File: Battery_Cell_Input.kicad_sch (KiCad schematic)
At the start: 3 parts, among them J801 Conn_01x02, J802 Conn_01x02, J803 Conn_01x02

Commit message: specified design
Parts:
- removed J801, J802: Conn_01x02, symbol Connector_Generic:Conn_01x02
- added BT1101, BT1102, BT1103, BT1104: Battery_Cell, symbol Device:Battery_Cell
- added C1101, C1102: C_Small, Capacitor_SMD:C_0603_1608Metric_Pad1.08x0.95mm_HandSolder, symbol Device:C_Small
- added D1101, D1102: 1N4148WT, Diode_SMD:D_SOD-523, symbol Diode:1N4148WT
- added J1101: Battery_1, Connector_Harwin:Harwin_Gecko-G125-FVX1605L0X_2x08_P1.25mm_Vertical, symbol Connector_Generic:Conn_02x08_Row_Letter_Last
- added Q1101, Q1102: NMOS, Package_TO_SOT_SMD:SOT-23-6, symbol Simulation_SPICE:NMOS
- added R1101, R1102: TBD, Resistor_SMD:R_0603_1608Metric_Pad0.98x0.95mm_HandSolder, symbol Device:R_Small
- added R1103, R1104, R1105, R1106, R1107, R1108, R1109, R1110, R1111, R1112, R1113, R1114: R_Small, Resistor_SMD:R_0603_1608Metric_Pad0.98x0.95mm_HandSolder, symbol Device:R_Small
- added U1101: BQ76920PW, Package_SO:TSSOP-20_4.4x6.5mm_P0.65mm, symbol Battery_Management:BQ76920PW
- J1102: renamed from J803; symbol Connector_Generic:Conn_01x02 -> Connector_Generic:Conn_01x04
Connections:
- net Batt: now also BT1101.1 (+), D1101.2 (A), D1102.2 (A), R1107.1
- net GND: now also J1102.2 (Pin_2), C1101.2, C1102.2, J1101.3a (Pin_3a), J1101.3b (Pin_3b), J1101.4a (Pin_4a), J1101.4b (Pin_4b), J1101.6a (Pin_6a), J1101.6b (Pin_6b), Q1102.3 (S), R1101.1, R1102.1, R1109.2, R1114.2, U1101.3 (VSS)
- net Heater_EN: now also J1101.8a (Pin_8a), J1101.8b (Pin_8b)
- net VMEAS: now also J1101.7a (Pin_7a), J1101.7b (Pin_7b)
- new net: Q1101.3 (S), R1108.2, R1110.2, R1111.2
- new net: R1110.1, U1101.19 (SRN)
- new net: BT1103.2 (-), BT1104.1 (+), R1105.1
- new net: Q1101.1 (D), Q1102.1 (D)
- new net: BT1102.2 (-), BT1103.1 (+), R1104.1
- new net: BT1104.2 (-), R1106.1, R1108.1
- new net: BT1101.2 (-), BT1102.1 (+), R1103.1
- new net: C1101.1, R1112.2, U1101.9 (REGSRC)
- new net: D1102.1 (K), R1113.1
- new net: C1102.1, R1113.2, U1101.10 (BAT)
- new net: D1101.1 (K), R1112.1
- new net: R1107.2, U1101.13 (VC4)
- new net: R1109.1, U1101.17 (VC0)
- new net: R1106.2, U1101.18 (SRP)
- new net Batt_1: R1105.2, U1101.16 (VC1)
- new net Batt_2: R1104.2, U1101.15 (VC2)
- new net Batt_3: R1103.2, U1101.14 (VC3)
- new net CHG: Q1102.2 (G), R1114.1, U1101.2 (CHG)
- new net DSG: Q1101.2 (G), R1111.1, U1101.1 (DSG)
- new net Pack: J1101.1a (Pin_1a), J1101.1b (Pin_1b), J1101.2a (Pin_2a), J1101.2b (Pin_2b)
- new net Switch_Batt_Heater/ILIM_1: R1102.2
- new net Switch_Batt_Heater/ILIM_2: R1101.2
- new net Switch_Batt_Heater/VOUT: J1102.3 (Pin_3), J1102.4 (Pin_4)
- new net TMEAS: J1101.5a (Pin_5a), J1101.5b (Pin_5b)
- no-connect marks 0 -> 4
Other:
- added sheet Switch_Batt_Heater (Switch_H.kicad_sch)
- added sheet Temp_sens_battery (Temp_sens.kicad_sch)
- note added: "Current limiter"
- note removed: "Batt heater"
- note removed: "Charger"
- note removed: "Temp Sens Batt"
- note removed: "Temp Sens Charger"
- note removed: "Temp sens Conn"

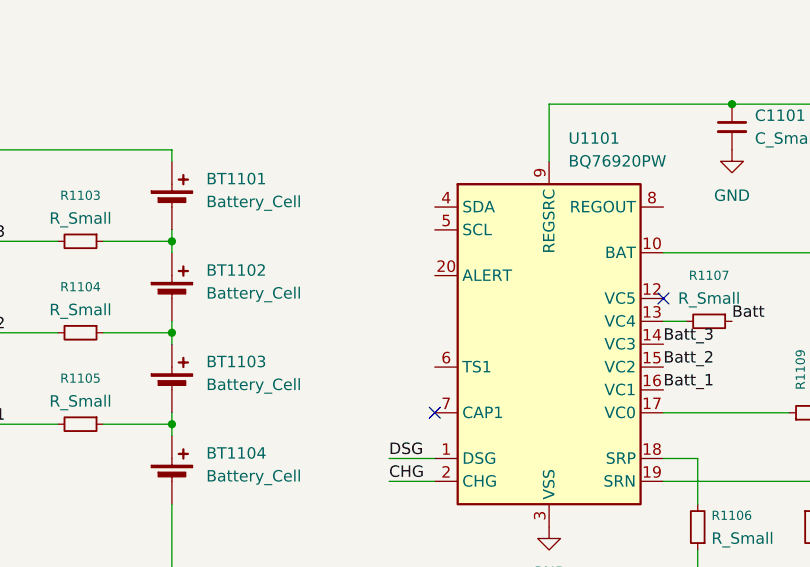
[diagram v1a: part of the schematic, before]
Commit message: added second AMUX and housekeeping
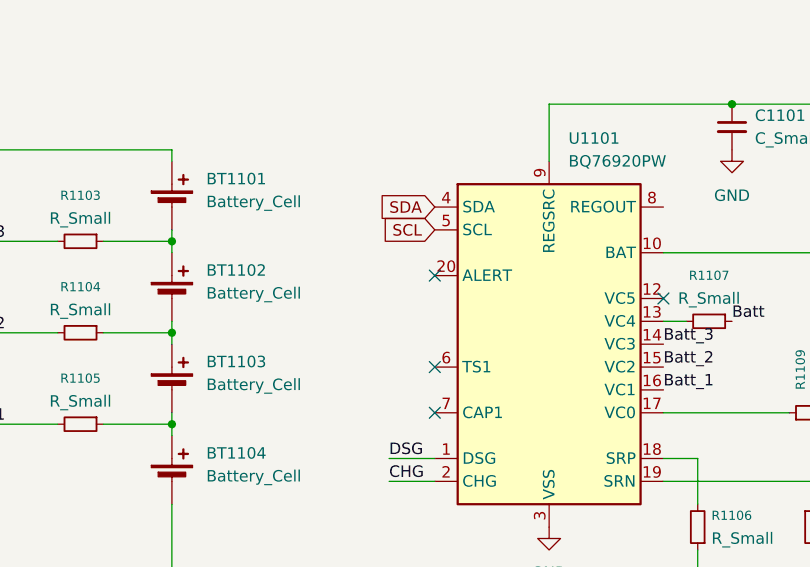
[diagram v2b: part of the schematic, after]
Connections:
- net SDA: now reaches U1101.4 (SDA)
- net SCL: now reaches U1101.5 (SCL)
- no-connect marks 4 -> 6
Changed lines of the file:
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@@
+	)
+	(no_connect
+		(at 175.26 113.03)
 	)
 	(no_connect
 		(at 175.26 128.27)
+	)
+	(no_connect
+		(at 175.26 123.19)
 	)
 	(no_connect
@@
 		)
 	)
+	(global_label "SDA"
+		(shape input)
+		(at 175.26 105.41 180)
+		(fields_autoplaced yes)
+		(effects
+			(font
+				(size 1.27 1.27)
+			)
+			(justify right)
+		)
+		(property "Intersheetrefs" "${INTERSHEET_REFS}"
+			(at 168.7067 105.41 0)
+			(effects
+				(font
+					(size 1.27 1.27)
+				)
+				(justify right)
+				(hide yes)
+			)
+		)
+		(property "Netclass" "I2C"
+			(at 175.26 107.6008 0)
+			(effects
+				(font
+					(size 1.27 1.27)
+				)
+				(justify right)
+				(hide yes)
+			)
+		)
+	)
+	(global_label "SCL"
+		(shape input)
+		(at 175.26 107.95 180)
+		(fields_autoplaced yes)
+		(effects
+			(font
+				(size 1.27 1.27)
+			)
+			(justify right)
+		)
+		(property "Intersheetrefs" "${INTERSHEET_REFS}"
+			(at 168.7672 107.95 0)
+			(effects
+				(font
+					(size 1.27 1.27)
+				)
+				(justify right)
+				(hide yes)
+			)
+		)
+		(property "Netclass" "I2C"
+			(at 175.26 110.1408 0)
+			(effects
+				(font
+					(size 1.27 1.27)
+				)
+				(justify right)
+				(hide yes)
+			)
+		)
+	)

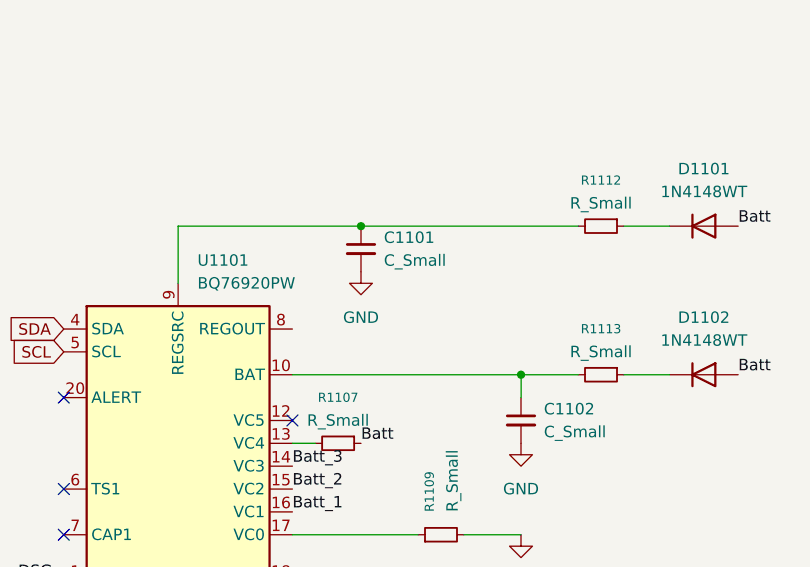
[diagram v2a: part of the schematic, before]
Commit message: changed IO epanders to 2nd MSP430
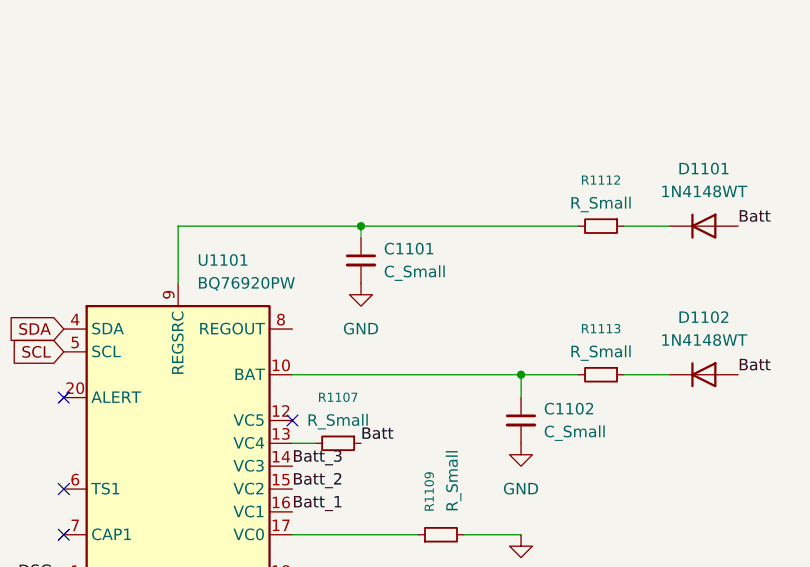
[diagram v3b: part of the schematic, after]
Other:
- moved on the sheet: C1101
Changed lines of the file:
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@@
+	(wire
+		(pts
+			(xy 208.28 95.25) (xy 208.28 93.98)
+		)
+		(stroke
+			(width 0)
+			(type default)
+		)
+	)
 	(wire
 		(pts
@@
 	(symbol
 		(lib_id "power:GND")
-		(at 208.28 99.06 0)
+		(at 208.28 100.33 0)
 		(unit 1)
 		(exclude_from_sim no)
@@
 		(fields_autoplaced yes)
 		(property "Reference" "#PWR01107"
+			(at 208.28 106.68 0)
+			(effects
+				(font
+					(size 1.27 1.27)
+				)
+				(hide yes)
+			)
+		)
+		(property "Value" "GND"
 			(at 208.28 105.41 0)
 			(effects
@@
 					(size 1.27 1.27)
 				)
-				(hide yes)
-			)
-		)
-		(property "Value" "GND"
-			(at 208.28 104.14 0)
-			(effects
-				(font
-					(size 1.27 1.27)
-				)
 			)
 		)
 		(property "Footprint" ""
-			(at 208.28 99.06 0)
+			(at 208.28 100.33 0)
 			(effects
 				(font
@@
 		)
 		(property "Datasheet" ""
-			(at 208.28 99.06 0)
+			(at 208.28 100.33 0)
 			(effects
 				(font
@@
 		)
 		(property "Description" "Power symbol creates a global label with name \"GND\" , ground"
-			(at 208.28 99.06 0)
+			(at 208.28 100.33 0)
 			(effects
 				(font
@@
 	(symbol
 		(lib_id "Device:C_Small")
-		(at 208.28 96.52 0)
+		(at 208.28 97.79 0)
 		(unit 1)
 		(exclude_from_sim no)
@@
 		(fields_autoplaced yes)
 		(property "Reference" "C1101"
-			(at 210.82 95.2562 0)
+			(at 210.82 96.5262 0)
 			(effects
 				(font
@@
 		)
 		(property "Value" "C_Small"
-			(at 210.82 97.7962 0)
+			(at 210.82 99.0662 0)
 			(effects
 				(font
@@
 		)
 		(property "Footprint" "Capacitor_SMD:C_0603_1608Metric_Pad1.08x0.95mm_HandSolder"
-			(at 208.28 96.52 0)
+			(at 208.28 97.79 0)
 			(effects
 				(font
@@
 		)
 		(property "Datasheet" "~"
-			(at 208.28 96.52 0)
+			(at 208.28 97.79 0)
 			(effects
 				(font
@@
 		)
 		(property "Description" "Unpolarized capacitor, small symbol"
-			(at 208.28 96.52 0)
-			(effects
-				(font
+			(at 208.28 97.79 0)
+			(effects
+				(font

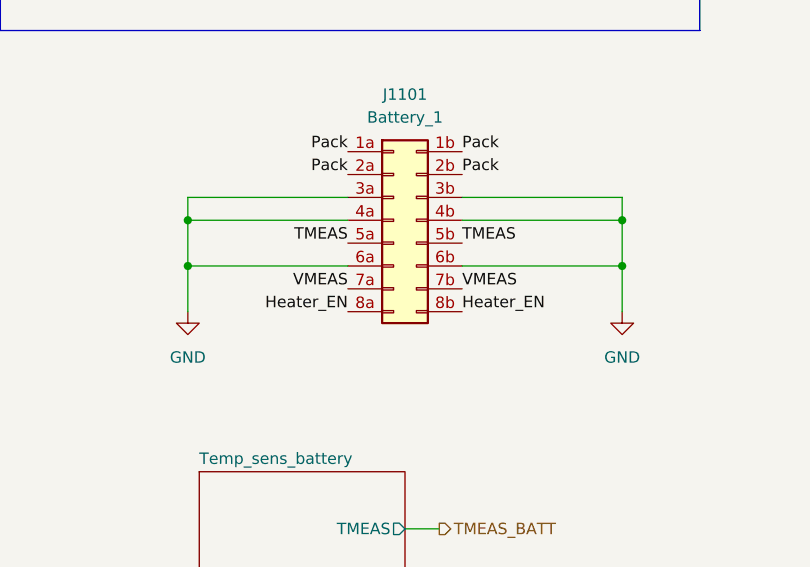
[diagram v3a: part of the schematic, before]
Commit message: added RS422, housekeeping
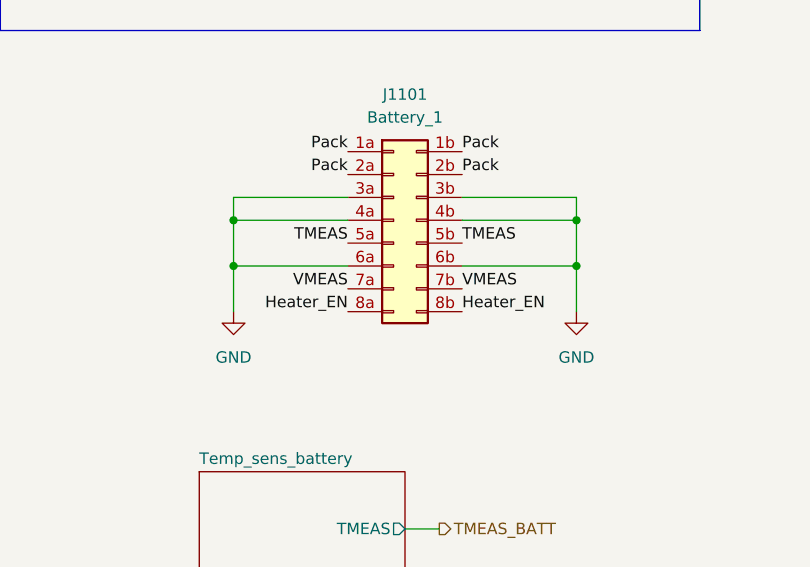
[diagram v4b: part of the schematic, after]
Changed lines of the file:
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@@
 	)
 	(junction
-		(at 38.1 91.44)
+		(at 43.18 91.44)
 		(diameter 0)
 		(color 0 0 0 0)
@@
 	)
 	(junction
-		(at 38.1 96.52)
+		(at 43.18 96.52)
 		(diameter 0)
 		(color 0 0 0 0)
@@
 	)
 	(junction
-		(at 86.36 91.44)
+		(at 81.28 91.44)
 		(diameter 0)
 		(color 0 0 0 0)
@@
 	)
 	(junction
-		(at 86.36 96.52)
+		(at 81.28 96.52)
 		(diameter 0)
 		(color 0 0 0 0)
@@
 	(wire
 		(pts
-			(xy 86.36 96.52) (xy 86.36 91.44)
+			(xy 81.28 96.52) (xy 81.28 91.44)
 		)
 		(stroke
@@
 	(wire
 		(pts
-			(xy 38.1 88.9) (xy 55.88 88.9)
+			(xy 43.18 88.9) (xy 55.88 88.9)
 		)
 		(stroke
@@
 	(wire
 		(pts
-			(xy 86.36 101.6) (xy 86.36 96.52)
+			(xy 81.28 101.6) (xy 81.28 96.52)
 		)
 		(stroke
@@
 	(wire
 		(pts
-			(xy 68.58 96.52) (xy 86.36 96.52)
+			(xy 68.58 96.52) (xy 81.28 96.52)
 		)
 		(stroke
@@
 	(wire
 		(pts
-			(xy 68.58 88.9) (xy 86.36 88.9)
+			(xy 68.58 88.9) (xy 81.28 88.9)
 		)
 		(stroke
@@
 	(wire
 		(pts
-			(xy 38.1 101.6) (xy 38.1 96.52)
+			(xy 43.18 101.6) (xy 43.18 96.52)
 		)
 		(stroke
@@
 	(wire
 		(pts
-			(xy 38.1 96.52) (xy 55.88 96.52)
+			(xy 43.18 96.52) (xy 55.88 96.52)
 		)
 		(stroke
@@
 	(wire
 		(pts
-			(xy 38.1 91.44) (xy 55.88 91.44)
+			(xy 43.18 91.44) (xy 55.88 91.44)
 		)
 		(stroke
@@
 	(wire
 		(pts
-			(xy 38.1 96.52) (xy 38.1 91.44)
+			(xy 43.18 96.52) (xy 43.18 91.44)
 		)
 		(stroke
@@
 	(wire
 		(pts
-			(xy 68.58 91.44) (xy 86.36 91.44)
+			(xy 68.58 91.44) (xy 81.28 91.44)
 		)
 		(stroke
@@
 	(wire
 		(pts
-			(xy 38.1 88.9) (xy 38.1 91.44)
+			(xy 43.18 88.9) (xy 43.18 91.44)
 		)
 		(stroke
@@
 	(wire
 		(pts
-			(xy 86.36 88.9) (xy 86.36 91.44)
+			(xy 81.28 88.9) (xy 81.28 91.44)
 		)
 		(stroke
@@
 	(symbol
 		(lib_id "power:GND")
-		(at 86.36 101.6 0)
+		(at 81.28 101.6 0)
 		(unit 1)
 		(exclude_from_sim no)
@@
 		(fields_autoplaced yes)
 		(property "Reference" "#PWR01105"
-			(at 86.36 107.95 0)
+			(at 81.28 107.95 0)
 			(effects
 				(font
@@
 		)
 		(property "Value" "GND"
-			(at 86.36 106.68 0)
+			(at 81.28 106.68 0)
 			(effects
 				(font
@@
 		)
 		(property "Footprint" ""
-			(at 86.36 101.6 0)
+			(at 81.28 101.6 0)
 			(effects
 				(font
@@
 		)
 		(property "Datasheet" ""
-			(at 86.36 101.6 0)
+			(at 81.28 101.6 0)
 			(effects
 				(font
@@
 		)
 		(property "Description" "Power symbol creates a global label with name \"GND\" , ground"
-			(at 86.36 101.6 0)
+			(at 81.28 101.6 0)
 			(effects
 				(font
@@
 	(symbol
 		(lib_id "power:GND")
-		(at 38.1 101.6 0)
+		(at 43.18 101.6 0)
 		(unit 1)
 		(exclude_from_sim no)
@@
 		(fields_autoplaced yes)
 		(property "Reference" "#PWR01101"
-			(at 38.1 107.95 0)
+			(at 43.18 107.95 0)
 			(effects
 				(font
@@
 		)
 		(property "Value" "GND"
-			(at 38.1 106.68 0)
+			(at 43.18 106.68 0)
 			(effects
 				(font
@@
 		)
 		(property "Footprint" ""
-			(at 38.1 101.6 0)
+			(at 43.18 101.6 0)
 			(effects
 				(font
@@
 		)
 		(property "Datasheet" ""
-			(at 38.1 101.6 0)
+			(at 43.18 101.6 0)
 			(effects
 				(font
@@
 		)
 		(property "Description" "Power symbol creates a global label with name \"GND\" , ground"
-			(at 38.1 101.6 0)
+			(at 43.18 101.6 0)
 			(effects
 				(font
